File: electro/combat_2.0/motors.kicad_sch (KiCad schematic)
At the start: 9 parts, among them J2 MOT_A, J3 MOT_B, U3 TB6612FNG

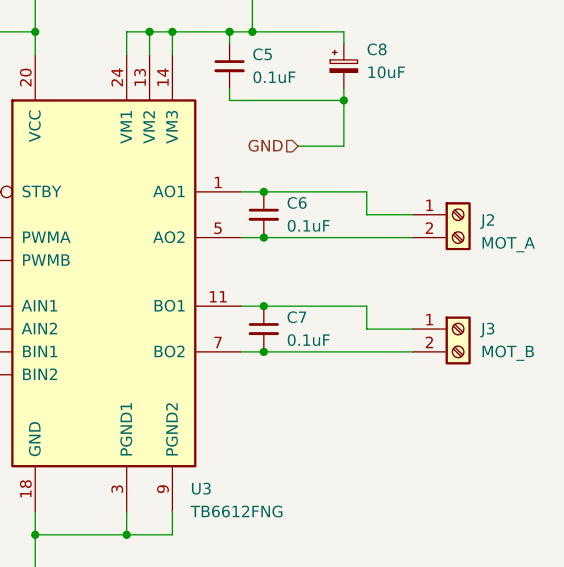
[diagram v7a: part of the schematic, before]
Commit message: change connectors
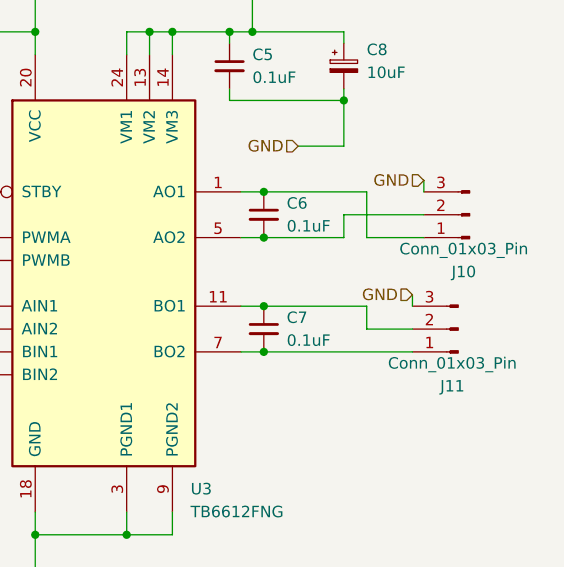
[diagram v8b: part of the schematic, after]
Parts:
- removed J2: MOT_A, TerminalBlock:TerminalBlock_Altech_AK300-2_P5.00mm, symbol Connector:Screw_Terminal_01x02
- removed J3: MOT_B, TerminalBlock:TerminalBlock_Altech_AK300-2_P5.00mm, symbol Connector:Screw_Terminal_01x02
- added J10, J11: Conn_01x03_Pin, Connector_JST:JST_GH_SM02B-GHS-TB_1x02-1MP_P1.25mm_Horizontal, symbol Connector:Conn_01x03_Pin
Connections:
- net GND: now also J10.3 (Pin_3), J11.3 (Pin_3)
- net at C6.1, U3.1 (AO1), U3.2 (AO1): now also J10.1 (Pin_1)
- net at C7.1, U3.11 (BO1), U3.12 (BO1): now also J11.2 (Pin_2)
- net at C6.2, U3.5 (AO2), U3.6 (AO2): now also J10.2 (Pin_2)
- net at C7.2, U3.7 (BO2), U3.8 (BO2): now also J11.1 (Pin_1)
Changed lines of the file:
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@@
   (junction (at 123.19 33.02) (diameter 0) (color 0 0 0 0)
   )
+  (junction (at 124.46 55.88) (diameter 0) (color 0 0 0 0)
+  )
+  (junction (at 124.46 68.58) (diameter 0) (color 0 0 0 0)
+  )
   (junction (at 120.65 33.02) (diameter 0) (color 0 0 0 0)
   )
   (junction (at 133.35 40.64) (diameter 0) (color 0 0 0 0)
   )
-  (junction (at 124.46 55.88) (diameter 0) (color 0 0 0 0)
-  )
   (junction (at 111.76 33.02) (diameter 0) (color 0 0 0 0)
   )
   (junction (at 81.28 33.02) (diameter 0) (color 0 0 0 0)
   )
-  (junction (at 124.46 68.58) (diameter 0) (color 0 0 0 0)
-  )
   (junction (at 109.22 88.9) (diameter 0) (color 0 0 0 0)
   )
@@
     (stroke (width 0) (type default))
   )
+  (wire (pts (xy 124.46 68.58) (xy 140.97 68.58))
+    (stroke (width 0) (type default))
+  )
   (wire (pts (xy 109.22 35.56) (xy 109.22 33.02))
     (stroke (width 0) (type default))
@@
     (stroke (width 0) (type default))
   )
+  (wire (pts (xy 142.24 53.34) (xy 133.35 53.34))
+    (stroke (width 0) (type default))
+  )
   (wire (pts (xy 81.28 33.02) (xy 81.28 35.56))
     (stroke (width 0) (type default))
@@
     (stroke (width 0) (type default))
   )
-  (wire (pts (xy 124.46 55.88) (xy 140.97 55.88))
-    (stroke (width 0) (type default))
-  )
   (wire (pts (xy 68.58 40.64) (xy 68.58 43.18))
     (stroke (width 0) (type default))
@@
     (stroke (width 0) (type default))
   )
+  (wire (pts (xy 133.35 55.88) (xy 124.46 55.88))
+    (stroke (width 0) (type default))
+  )
   (wire (pts (xy 99.06 88.9) (xy 99.06 86.36))
     (stroke (width 0) (type default))
@@
     (stroke (width 0) (type default))
   )
+  (wire (pts (xy 135.89 55.88) (xy 142.24 55.88))
+    (stroke (width 0) (type default))
+  )
   (wire (pts (xy 120.65 33.02) (xy 123.19 33.02))
     (stroke (width 0) (type default))
   )
-  (wire (pts (xy 135.89 53.34) (xy 135.89 50.8))
+  (wire (pts (xy 135.89 50.8) (xy 135.89 55.88))
     (stroke (width 0) (type default))
   )
@@
     (stroke (width 0) (type default))
   )
+  (wire (pts (xy 133.35 53.34) (xy 133.35 55.88))
+    (stroke (width 0) (type default))
+  )
   (wire (pts (xy 92.71 93.98) (xy 99.06 93.98))
     (stroke (width 0) (type default))
@@
     (stroke (width 0) (type default))
   )
-  (wire (pts (xy 124.46 68.58) (xy 140.97 68.58))
+  (wire (pts (xy 142.24 49.53) (xy 142.24 50.8))
     (stroke (width 0) (type default))
   )
@@
     (stroke (width 0) (type default))
   )
-  (wire (pts (xy 135.89 53.34) (xy 140.97 53.34))
-    (stroke (width 0) (type default))
-  )
   (wire (pts (xy 121.92 55.88) (xy 124.46 55.88))
     (stroke (width 0) (type default))
   )
+  (wire (pts (xy 135.89 66.04) (xy 140.97 66.04))
+    (stroke (width 0) (type default))
+  )
   (wire (pts (xy 133.35 40.64) (xy 133.35 39.37))
     (stroke (width 0) (type default))
@@
     (stroke (width 0) (type default))
   )
-  (wire (pts (xy 135.89 66.04) (xy 140.97 66.04))
+  (wire (pts (xy 140.97 62.23) (xy 140.97 63.5))
     (stroke (width 0) (type default))
   )
@@
     (effects (font (size 1.27 1.27)) (justify right))
   )
+  (hierarchical_label "GND" (shape input) (at 142.24 49.53 180) (fields_autoplaced)
+    (effects (font (size 1.27 1.27)) (justify right))
+  )
   (hierarchical_label "GND" (shape input) (at 128.27 45.72 180) (fields_autoplaced)
+    (effects (font (size 1.27 1.27)) (justify right))
+  )
+  (hierarchical_label "GND" (shape input) (at 140.97 62.23 180) (fields_autoplaced)
     (effects (font (size 1.27 1.27)) (justify right))
   )
@@
     )
   )
-  (symbol (lib_id "Connector:Screw_Terminal_01x02") (at 146.05 53.34 0) (unit 1)
-    (in_bom yes) (on_board yes) (dnp no) (fields_autoplaced)
-    (property "Reference" "J2" (at 148.59 53.975 0)
-      (effects (font (size 1.27 1.27)) (justify left))
-    )
-    (property "Value" "MOT_A" (at 148.59 56.515 0)
-      (effects (font (size 1.27 1.27)) (justify left))
-    )
-    (property "Footprint" "TerminalBlock:TerminalBlock_Altech_AK300-2_P5.00mm" (at 146.05 53.34 0)
-      (effects (font (size 1.27 1.27)) hide)
-    )
-    (property "Datasheet" "~" (at 146.05 53.34 0)
-      (effects (font (size 1.27 1.27)) hide)
-    )
-    (pin "1")
-    (pin "2")
-    (instances
-      (project "combat_2.0"
-        (path "/518cdd36-e3d2-496e-a534-90a14dea15b3/75a6c3bc-fc0f-431f-8cec-1b3bc24c24b9"
-          (reference "J2") (unit 1)
-        )
-      )
-    )
-  )
   (symbol (lib_id "Device:C_Polarized_Small") (at 133.35 36.83 0) (unit 1)
     (in_bom yes) (on_board yes) (dnp no) (fields_autoplaced)
@@
     )
   )
+  (symbol (lib_id "Connector:Conn_01x03_Pin") (at 147.32 53.34 180) (unit 1)
+    (in_bom yes) (on_board yes) (dnp no) (fields_autoplaced)
+    (property "Reference" "J10" (at 146.685 59.69 0)
+      (effects (font (size 1.27 1.27)))
+    )
+    (property "Value" "Conn_01x03_Pin" (at 146.685 57.15 0)
+      (effects (font (size 1.27 1.27)))
+    )
+    (property "Footprint" "Connector_JST:JST_GH_SM02B-GHS-TB_1x02-1MP_P1.25mm_Horizontal" (at 147.32 53.34 0)
+      (effects (font (size 1.27 1.27)) hide)
+    )
+    (property "Datasheet" "~" (at 147.32 53.34 0)
+      (effects (font (size 1.27 1.27)) hide)
+    )
+    (pin "1")
+    (pin "2")
+    (pin "3")
+    (instances
+      (project "combat_2.0"
+        (path "/518cdd36-e3d2-496e-a534-90a14dea15b3/75a6c3bc-fc0f-431f-8cec-1b3bc24c24b9"
+          (reference "J10") (unit 1)
+        )
+      )
+    )
+  )
   (symbol (lib_id "Device:C_Small") (at 124.46 53.34 0) (unit 1)
     (in_bom yes) (on_board yes) (dnp no) (fields_autoplaced)
@@
     )
   )
-  (symbol (lib_id "Connector:Screw_Terminal_01x02") (at 146.05 66.04 0) (unit 1)
-    (in_bom yes) (on_board yes) (dnp no) (fields_autoplaced)
-    (property "Reference" "J3" (at 148.59 66.0399 0)
-      (effects (font (size 1.27 1.27)) (justify left))
-    )
-    (property "Value" "MOT_B" (at 148.59 68.5799 0)
-      (effects (font (size 1.27 1.27)) (justify left))
-    )
-    (property "Footprint" "TerminalBlock:TerminalBlock_Altech_AK300-2_P5.00mm" (at 146.05 66.04 0)
+  (symbol (lib_id "Connector:Conn_01x03_Pin") (at 146.05 66.04 180) (unit 1)
+    (in_bom yes) (on_board yes) (dnp no) (fields_autoplaced)
+    (property "Reference" "J11" (at 145.415 72.39 0)
+      (effects (font (size 1.27 1.27)))
+    )
+    (property "Value" "Conn_01x03_Pin" (at 145.415 69.85 0)
+      (effects (font (size 1.27 1.27)))
+    )
+    (property "Footprint" "Connector_JST:JST_GH_SM02B-GHS-TB_1x02-1MP_P1.25mm_Horizontal" (at 146.05 66.04 0)
       (effects (font (size 1.27 1.27)) hide)
     )
@@
     (pin "1")
     (pin "2")
-    (instances
-      (project "combat_2.0"
-        (path "/518cdd36-e3d2-496e-a534-90a14dea15b3/75a6c3bc-fc0f-431f-8cec-1b3bc24c24b9"
-          (reference "J3") (unit 1)
-        )
-      )
+    (pin "3")
+    (instances
+      (project "combat_2.0"
+        (path "/518cdd36-e3d2-496e-a534-90a14dea15b3/75a6c3bc-fc0f-431f-8cec-1b3bc24c24b9"
+          (reference "J11") (unit 1)
+        )
+      )
